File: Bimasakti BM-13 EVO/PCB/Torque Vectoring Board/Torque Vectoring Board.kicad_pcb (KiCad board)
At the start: 2 copper layers, 108 x 110 mm, 30 parts, among them U3 SN65HVD230, U4 SN65HVD230, U5 ADS1115IDGS

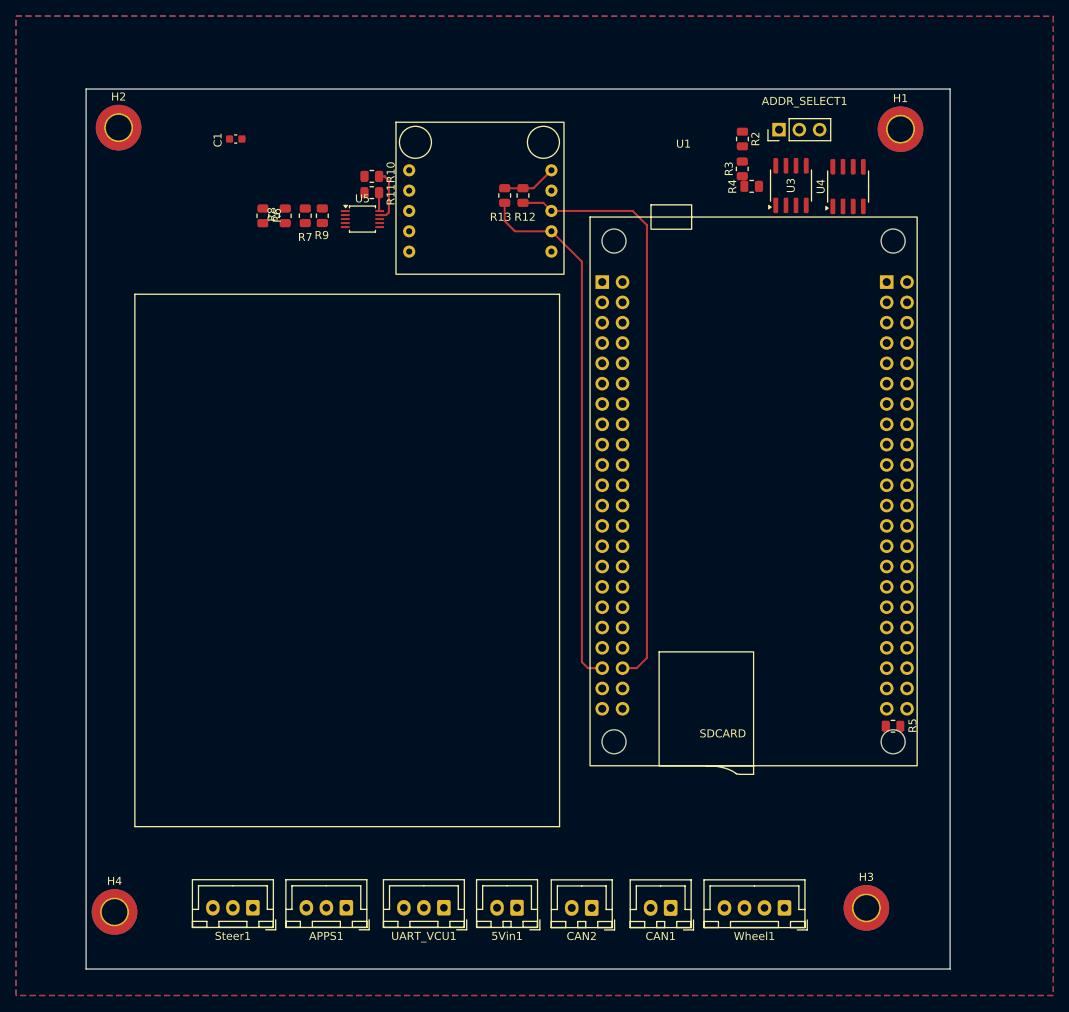
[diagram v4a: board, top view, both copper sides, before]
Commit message: pdm selesai ril, tv board sudah bagus kurang cek (mungkin ganti konektor)
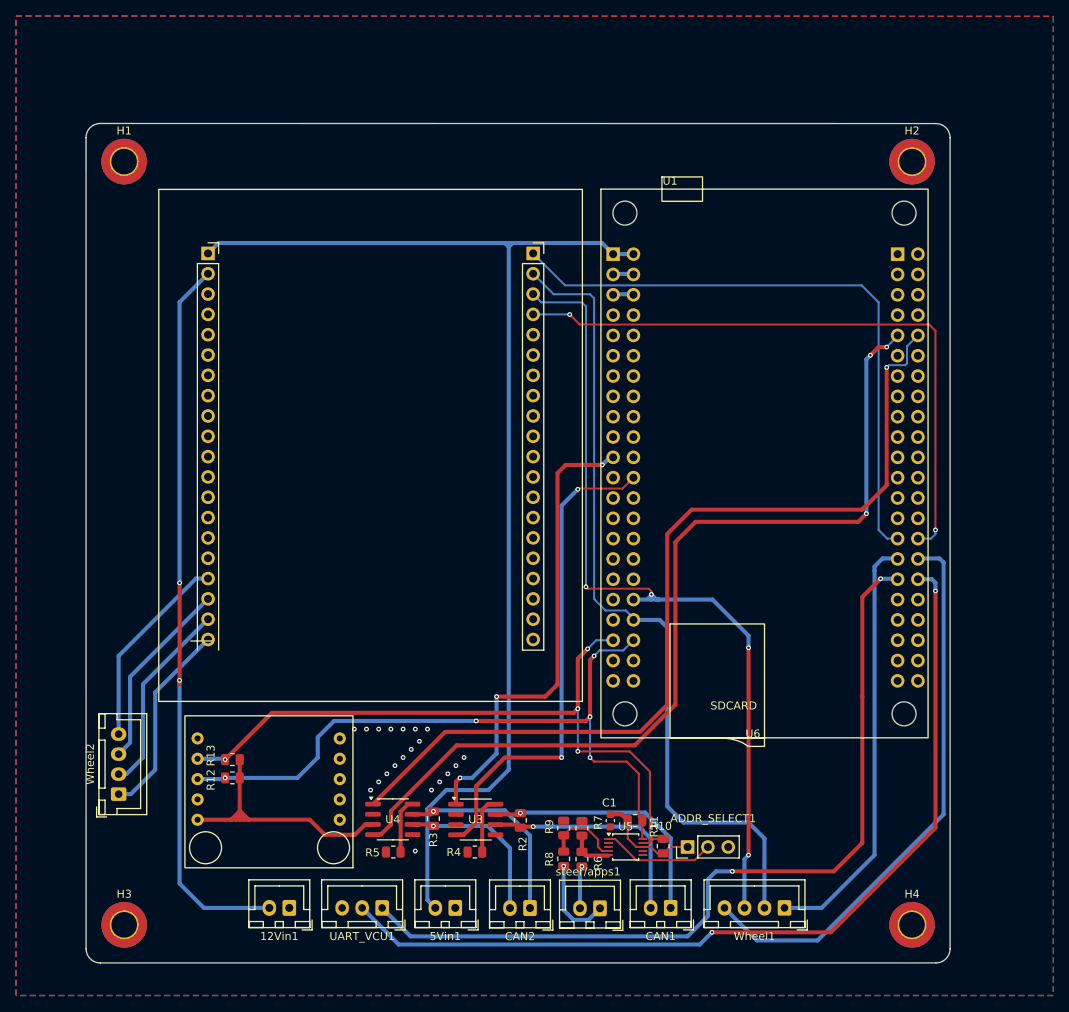
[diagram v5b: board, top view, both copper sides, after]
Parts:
- removed APPS1, Steer1: Conn_01x03, Connector_JST:JST_XH_B3B-XH-A_1x03_P2.50mm_Vertical
- added 12Vin1: Conn_01x02, Connector_JST:JST_XH_B2B-XH-A_1x02_P2.50mm_Vertical, F.Cu at (70.1, 131.6)
- added U6: ~, 0_CUSTOM_PCB:wheelspeed, F.Cu at (80.3, 36.7)
- added Wheel2: Conn_01x04, Connector_JST:JST_XH_B4B-XH-A_1x04_P2.50mm_Vertical, F.Cu at (48.8, 117.3)
- added steer/apps1: Conn_01x02, Connector_JST:JST_XH_B2B-XH-A_1x02_P2.50mm_Vertical, F.Cu at (108.9, 131.6)
- moved U2 111.8 mm to (66.6, 134.0), turned to 180 degrees
- moved H4 99.7 mm to (147.9, 133.7)
- moved H2 99.3 mm to (147.9, 38.3)
- moved U4 97.4 mm to (83.0, 120.5), turned to 0 degrees
- moved C1 97.2 mm to (110.2, 120.7), turned to 90 degrees
- moved H1 97.1 mm to (49.5, 38.3)
- moved H3 92.8 mm to (49.5, 133.7)
- moved R10 91.3 mm to (116.8, 123.8), turned to 90 degrees
- moved ADDR_SELECT1 90.4 mm to (119.9, 124.0)
- moved R4 90.1 mm to (93.3, 124.6)
- moved R3 89.9 mm to (88.1, 120.4), turned to -90 degrees
- moved R6 89.8 mm to (106.7, 125.5)
- moved R2 89.6 mm to (99.0, 120.6)
- moved U3 88.5 mm to (93.4, 120.5), turned to 0 degrees
- moved R8 87.6 mm to (104.4, 125.4), turned to 90 degrees
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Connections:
- U1 pad 2: unconnected-(U1-5V-Pad2) -> 5V
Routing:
- net SS: track 0.00 -> 149.3 mm, vias 0 -> 2
- net 5V: track 0.00 -> 146.1 mm
- net SCK: track 0.00 -> 130.5 mm
- net CAN2_RX: track 0.00 -> 115.7 mm, vias 0 -> 3
- net CAN2_TX: track 0.00 -> 114.8 mm, vias 0 -> 1
- net RX1: track 0.00 -> 112.6 mm, vias 0 -> 2
- net MOSI: track 0.00 -> 107.3 mm, vias 0 -> 4
- net TX1: track 0.00 -> 105.1 mm, vias 0 -> 2
- net MISO: track 0.00 -> 101.9 mm
- net 12V: track 0.00 -> 90.7 mm, vias 0 -> 2
- net CAN1_RX: track 0.00 -> 61.8 mm, vias 0 -> 2
- net CAN1_TX: track 0.00 -> 58.9 mm, vias 0 -> 3
- net 3V3: track 6.77 -> 51.5 mm
- net CANH1: track 0.00 -> 32.0 mm, vias 0 -> 1
- net CANL1: track 0.00 -> 28.9 mm, vias 0 -> 1
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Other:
- board size 108 x 110 mm -> 108 x 104.9 mm

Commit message: buat placeholder baru dan ganti konektor
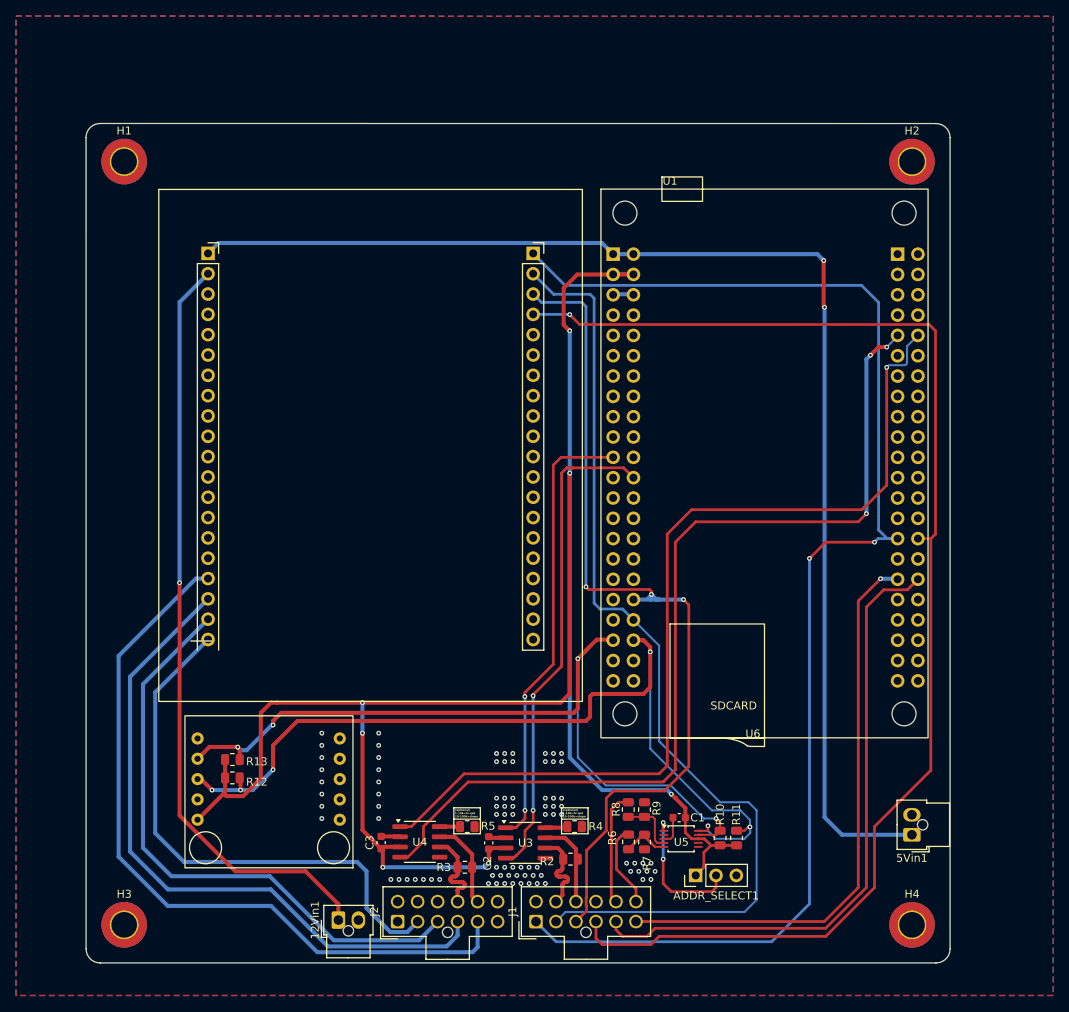
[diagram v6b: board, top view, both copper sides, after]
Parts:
- removed CAN1, CAN2, steer/apps1: Conn_01x02, Connector_JST:JST_XH_B2B-XH-A_1x02_P2.50mm_Vertical
- removed UART_VCU1: Conn_01x03, Connector_JST:JST_XH_B3B-XH-A_1x03_P2.50mm_Vertical
- removed Wheel1, Wheel2: Conn_01x04, Connector_JST:JST_XH_B4B-XH-A_1x04_P2.50mm_Vertical
- added C2: 0.1uF, Capacitor_SMD:C_0603_1608Metric, F.Cu at (95.0, 123.4)
- added C3: 0.1uF, Capacitor_SMD:C_0603_1608Metric, F.Cu at (81.6, 123.4)
- added J1: SIGNAL 1, Connector_Molex:Molex_Nano-Fit_105310-xx12_2x06_P2.50mm_Vertical, F.Cu at (100.9, 133.3)
- added J2: SIGNAL 1, Connector_Molex:Molex_Nano-Fit_105310-xx12_2x06_P2.50mm_Vertical, F.Cu at (83.6, 133.3)
- 12Vin1, 5Vin1: footprint Connector_JST:JST_XH_B2B-XH-A_1x02_P2.50mm_Vertical -> Connector_Molex:Molex_Nano-Fit_105309-xx02_1x02_P2.50mm_Vertical
- moved 5Vin1 57.8 mm to (147.9, 122.4)
- moved R11 12.9 mm to (126.0, 122.8), turned to 90 degrees
- moved R4 12.9 mm to (105.8, 121.4), turned to 180 degrees
- moved R9 10.4 mm to (114.5, 119.3)
- moved R8 10.2 mm to (112.5, 119.3), turned to -90 degrees
- moved R5 9.78 mm to (92.4, 121.4), turned to 180 degrees
- moved C1 8.61 mm to (118.8, 120.3), turned to 0 degrees
- moved R7 8.01 mm to (114.5, 123.3), turned to 90 degrees
- moved R2 7.92 mm to (105.3, 125.5), turned to 180 degrees
- moved R3 7.23 mm to (92.1, 126.5), turned to 180 degrees
- moved R10 7.18 mm to (124.0, 122.8)
- moved U5 7.00 mm to (119.1, 122.9)
- moved U3 6.88 mm to (99.6, 123.4)
- moved 12Vin1 6.32 mm to (76.2, 133.1), turned to 90 degrees
- moved R6 6.21 mm to (112.5, 123.3), turned to -90 degrees
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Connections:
- 12Vin1 pad 1: GND -> 12V
- 12Vin1 pad 2: 12V -> GND
- 5Vin1 pad 1: GND -> 5V
- 5Vin1 pad 2: 5V -> GND
- R6 pad 1: Net-(steer/apps1-Pin_2) -> APPS_IN
- R8 pad 1: Net-(steer/apps1-Pin_1) -> STEER_IN
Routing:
- net 3V3: track 51.5 -> 234.7 mm, vias 0 -> 7
- net WS_FR: track 25.0 -> 93.6 mm
- net WS_FL: track 24.0 -> 83.8 mm
- net WS_RR: track 24.6 -> 74.5 mm
- net WS_RL: track 24.8 -> 68.1 mm
- net SCK: track 130.5 -> 169.4 mm, vias 0 -> 2
- net RX1: track 112.6 -> 78.1 mm, vias 2 -> 0
- net TX1: track 105.1 -> 71.5 mm, vias 2 -> 1
- net SCL: track 87.7 -> 115.5 mm, vias 5 -> 6
- net CANH1: track 32.0 -> 11.0 mm, vias 1 -> 0
- net MISO: track 101.9 -> 122.4 mm
- net CANL1: track 28.9 -> 10.9 mm, vias 1 -> 0
- net SS: track 149.3 -> 165.7 mm, vias 2 -> 1
- net STEER_IN: track 0.00 -> 14.3 mm
- net CANH2: track 25.2 -> 11.2 mm, vias 1 -> 0
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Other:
- board text added: "(optional) 1-10k=hi spd 10-100k=slope"

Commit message: assembly kurang pneumatic, kurang wiring dudukan motherboard
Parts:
- added R14: 5K, Resistor_SMD:R_0805_2012Metric, F.Cu at (112.8, 126.9)
- added R15: 3K3, Resistor_SMD:R_0805_2012Metric, F.Cu at (114.8, 126.9)
- J2: value SIGNAL 1 -> SIGNAL 2
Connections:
- net APPS renamed APPS2
- net CANH1 renamed ESC1_HI
- net CANH2 renamed ESC2_HI
- net CANL1 renamed ESC1_LO
- net CANL2 renamed ESC2_LO
- net RX1 renamed STM_TX
- net TX1 renamed STM_RX
- J1 pad 10: unconnected-(J1-Pin_10-Pad10) -> STEER_IN
- J1 pad 11: STEER_IN -> APPS_IN2
- J1 pad 12: APPS_IN -> APPS_IN1
- R6 pad 1: APPS_IN -> APPS_IN2
- U5 pad 6: unconnected-(U5-AIN2-Pad6) -> APPS1
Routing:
- net APPS_IN: track 10.4 -> 0.00 mm
- net APPS1: track 0.00 -> 10.1 mm
- net APPS_IN2: track 0.00 -> 9.45 mm
- net APPS_IN1: track 0.00 -> 5.98 mm
- net STEER_IN: track 14.3 -> 14.8 mm
- net GND: vias 84 -> 79

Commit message: detailing
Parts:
- moved R5 0.40 mm to (91.9, 121.4)
- moved C3 0.33 mm to (81.9, 123.4)
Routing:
- net SDA: track 101.9 -> 101.3 mm
- net 3V3: track 234.7 -> 234.0 mm
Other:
- board text added: "+12"
- board text added: "GND"
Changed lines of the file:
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@@
 	(footprint "Resistor_SMD:R_0805_2012Metric"
 		(layer "F.Cu")
-		(at 92.3525 121.412 180)
+		(at 91.948 121.412 180)
 		(descr "Resistor SMD 0805 (2012 Metric), square (rectangular) end terminal, IPC-7351 nominal, (Body size source: IPC-SM-782 page 72, https://www.pcb-3d.com/wordpress/wp-content/uploads/ipc-sm-782a_amendment_1_and_2.pdf), generated with kicad-footprint-generator")
 		(tags "resistor")
@@
 		(tags "resistor")
 		(property "Reference" "R3"
-			(at 2.6435 0 0)
+			(at 0.013611 1.563886 0)
 			(layer "F.SilkS")
 			(effects
 				(font
-					(size 1 1)
-					(thickness 0.15)
+					(size 0.8 0.8)
+					(thickness 0.1)
 				)
 			)
@@
 	(footprint "Capacitor_SMD:C_0603_1608Metric"
 		(layer "F.Cu")
-		(at 81.588472 123.407759 90)
+		(at 81.921966 123.402231 90)
 		(descr "Capacitor SMD 0603 (1608 Metric), square (rectangular) end terminal, IPC-7351 nominal, (Body size source: IPC-SM-782 page 76, https://www.pcb-3d.com/wordpress/wp-content/uploads/ipc-sm-782a_amendment_1_and_2.pdf), generated with kicad-footprint-generator")
 		(tags "capacitor")
 		(property "Reference" "C3"
-			(at 0 -1.43 90)
+			(at -2.073769 0.036156 90)
 			(layer "F.SilkS")
 			(effects
 				(font
-					(size 1 1)
-					(thickness 0.15)
+					(size 0.8 0.8)
+					(thickness 0.1)
 				)
 			)
@@
 		)
 	)
+	(gr_rect
+		(start 80.772 119.014743)
+		(end 93.558255 127.33549)
+		(stroke
+			(width 0.1)
+			(type default)
+		)
+		(fill no)
+		(layer "F.SilkS")
+	)
 	(gr_line
-		(start 90.683013 120.471892)
-		(end 93.94845 120.471892)
+		(start 77.487765 129.735793)
+		(end 77.487765 131.246)
+		(stroke
+			(width 0.1)
+			(type default)
+		)
+		(layer "F.SilkS")
+	)
+	(gr_line
+		(start 90.259939 120.494469)
+		(end 93.525376 120.494469)
 		(stroke
 			(width 0.1)
@@
 	)
 	(gr_rect
-		(start 90.670221 119.049436)
-		(end 93.98 122.301799)
+		(start 90.247147 119.072013)
+		(end 93.556926 122.324376)
 		(stroke
 			(width 0.1)
@@
 	)
 	(gr_rect
+		(start 74.41 129.735793)
+		(end 80.56553 131.246)
+		(stroke
+			(width 0.1)
+			(type default)
+		)
+		(fill no)
+		(layer "F.SilkS")
+	)
+	(gr_rect
 		(start 104.14 119.049436)
 		(end 107.449779 122.301799)
@@
 	)
 	(gr_text "(optional)\n1-10k=hi spd\n10-100k=slope	"
-		(at 90.809214 120.282592 0)
+		(at 90.38614 120.305169 0)
 		(layer "F.SilkS")
 		(effects
@@
 		)
 	)
+	(gr_text "+12"
+		(at 75.043911 130.740053 0)
+		(layer "F.SilkS")
+		(effects
+			(font
+				(size 0.6 0.6)
+				(thickness 0.12)
+				(bold yes)
+			)
+			(justify left bottom)
+		)
+	)
+	(gr_text "GND"
+		(at 77.609011 130.814765 0)
+		(layer "F.SilkS")
+		(effects
+			(font
+				(size 0.6 0.6)
+				(thickness 0.12)
+				(bold yes)
+			)
+			(justify left bottom)
+		)
+	)
 	(dimension
 		(type orthogonal)
@@
 	)
 	(segment
+		(start 83.95 123.952)
+		(end 82.147197 123.952)
+		(width 0.508)
+		(layer "F.Cu")
+		(net 38)
+	)
+	(segment
 		(start 104.401 54.095)
 		(end 106.106666 52.389334)
@@
 	)
 	(segment
+		(start 81.921966 126.358034)
+		(end 81.921966 124.177231)
+		(width 0.508)
+		(layer "F.Cu")
+		(net 38)
+	)
+	(segment
 		(start 126.429821 123.752182)
 		(end 126.482405 123.804766)
@@
 	)
 	(segment
+		(start 82.147197 123.952)
+		(end 81.921966 124.177231)
+		(width 0.508)
+		(layer "F.Cu")
+		(net 38)
+	)
+	(segment
 		(start 95.175587 124.079)
 		(end 95.036611 124.217976)
@@
 	)
 	(segment
-		(start 81.788 126.492)
-		(end 81.788 124.382287)
-		(width 0.508)
-		(layer "F.Cu")
-		(net 38)
-	)
-	(segment
 		(start 79.248 105.911)
 		(end 104.01846 105.911)
@@
 	)
 	(segment
-		(start 81.788 124.382287)
-		(end 81.588472 124.182759)
-		(width 0.508)
-		(layer "F.Cu")
-		(net 38)
-	)
-	(segment
 		(start 119.611834 122.151834)
 		(end 120.396 122.936)
@@
 	)
 	(segment
+		(start 82.055932 126.492)
+		(end 81.921966 126.358034)
+		(width 0.508)
+		(layer "F.Cu")
+		(net 38)
+	)
+	(segment
 		(start 118.364 117.856)
 		(end 117.856 117.348)
@@
 	)
 	(segment
-		(start 81.836671 123.93456)
-		(end 83.93256 123.93456)
-		(width 0.508)
-		(layer "F.Cu")
-		(net 38)
-	)
-	(segment
 		(start 97.158 124.079)
 		(end 95.175587 124.079)
@@
 	)
 	(segment
-		(start 81.588472 124.182759)
-		(end 81.836671 123.93456)
+		(start 82.09333 126.492)
+		(end 82.055932 126.492)
 		(width 0.508)
 		(layer "F.Cu")
@@
 	)
 	(via
-		(at 81.788 126.492)
+		(at 82.09333 126.492)
 		(size 0.6)
 		(drill 0.3)
@@
 	)
 	(segment
-		(start 94.996 125.984)
-		(end 94.488 126.492)
-		(width 0.508)
-		(layer "B.Cu")
-		(net 38)
-	)
-	(segment
 		(start 109.22 116.84)
 		(end 105.156 112.776)
@@
 	(segment
 		(start 94.488 126.492)
-		(end 81.788 126.492)
+		(end 94.996 125.984)
 		(width 0.508)
 		(layer "B.Cu")
@@
 	)
 	(segment
+		(start 82.09333 126.492)
+		(end 94.488 126.492)
+		(width 0.508)
+		(layer "B.Cu")
+		(net 38)
+	)
+	(segment
 		(start 117.856 117.348)
 		(end 117.348 116.84)
@@
 	)
 	(segment
-		(start 68.072 108.204)
-		(end 68.072 108.712)
-		(width 0.508)
-		(layer "F.Cu")
-		(net 84)
-	)
-	(segment
 		(start 63.51171 111.47071)
 		(end 63.5 111.459)
@@
 	)
 	(segment
-		(start 105.664 107.188)
-		(end 106.172 106.68)
-		(width 0.508)
-		(layer "F.Cu")
-		(net 84)
-	)
-	(segment
 		(start 106.172 100.416348)
 		(end 107.20972 99.378628)
@@
 	)
 	(segment
-		(start 69.088 107.188)
-		(end 105.664 107.188)
-		(width 0.508)
-		(layer "F.Cu")
-		(net 84)
-	)
-	(segment
 		(start 107.39928 99.172886)
 		(end 108.530552 98.041614)
@@
 	)
 	(segment
-		(start 69.088 107.188)
-		(end 68.072 108.204)
-		(width 0.508)
-		(layer "F.Cu")
-		(net 84)
-	)
-	(segment
 		(start 63.66193 111.47071)
 		(end 63.51171 111.47071)
@@
 	)
 	(segment
+		(start 106.172 106.68)
+		(end 105.664 107.188)
+		(width 0.508)
+		(layer "F.Cu")
+		(net 84)
+	)
+	(segment
 		(start 107.20972 99.378628)
 		(end 107.212107 99.378628)
@@
 	)
 	(segment
-		(start 106.172 106.68)
-		(end 106.172 100.416348)
+		(start 106.172 100.416348)
+		(end 106.172 106.68)
+		(width 0.508)
+		(layer "F.Cu")
+		(net 84)
+	)
+	(segment
+		(start 105.664 107.188)
+		(end 69.596 107.188)
 		(width 0.508)
 		(layer "F.Cu")
@@
 	)
 	(segment
+		(start 69.596 107.188)
+		(end 68.072 108.712)
+		(width 0.508)
+		(layer "F.Cu")
+		(net 84)
+	)
+	(segment
 		(start 110.51428 98.041614)
 		(end 110.582 98.109334)
@@
 	)
 	(segment
-		(start 63.66193 111.47071)
-		(end 64.05472 111.8635)
+		(start 68.048716 108.712)
+		(end 68.072 108.712)
 		(width 0.508)
 		(layer "B.Cu")
@@
 	)
 	(segment
-		(start 109.654 116.258)
-		(end 106.172 112.776)
-		(width 0.254)
-		(layer "B.Cu")
-		(net 84)
-	)
-	(segment
-		(start 64.770302 111.8635)
-		(end 67.921802 108.712)
+		(start 63.66193 111.47071)
+		(end 65.290006 111.47071)
 		(width 0.508)
 		(layer "B.Cu")
@@
 	)
 	(segment
-		(start 64.05472 111.8635)
-		(end 64.770302 111.8635)
-		(width 0.508)
+		(start 109.654 116.258)
+		(end 106.172 112.776)
+		(width 0.254)
 		(layer "B.Cu")
 		(net 84)
 	)
 	(segment
-		(start 67.921802 108.712)
-		(end 68.072 108.712)
+		(start 65.290006 111.47071)
+		(end 68.048716 108.712)
 		(width 0.508)
 		(layer "B.Cu")
